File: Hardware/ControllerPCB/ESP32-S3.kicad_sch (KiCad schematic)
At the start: 55 parts, among them J1 UJ20-C-H-G-SMT-1-P16-TR, J4 RJ45, J5 Conn_TagConnect_TC2030-NL_ESP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, J8 Micro_SD_Card, U1 ESP32-S3-WROOM-1, U5 WE-TVS-82400102, U7 AP7333-33SRG-7

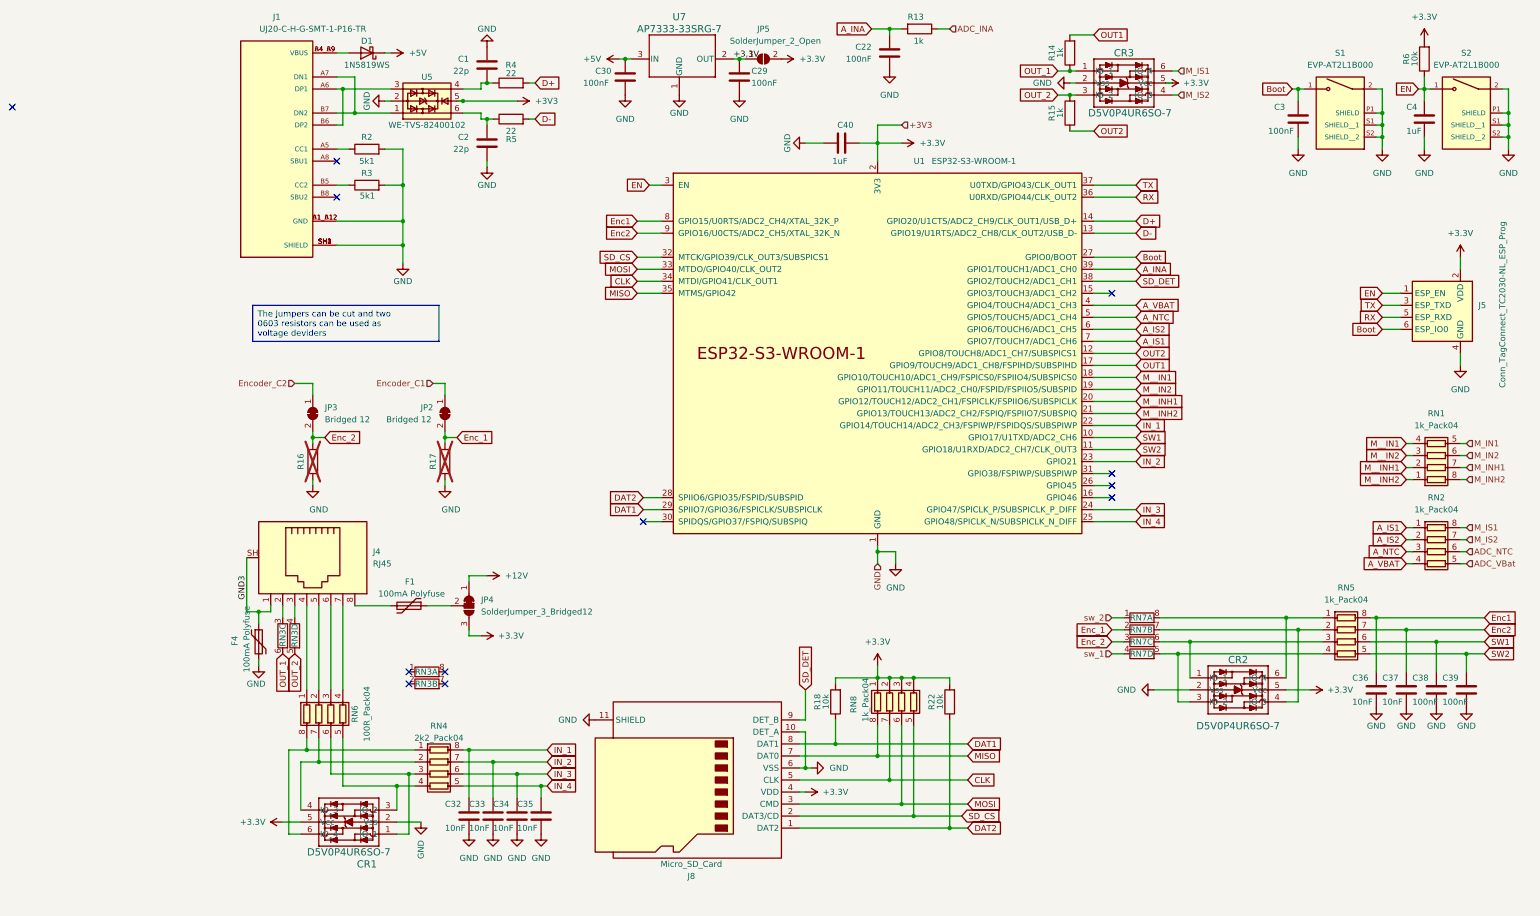
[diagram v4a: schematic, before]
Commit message: update Controller PCB
Add additional capacitor
fix footprint Resistor Array CAT16
fix 3D Model CAT16
change traces from 0.5 to 0.4 mm
fix USB-C Footprint
Export Gerber
update BOM and Values
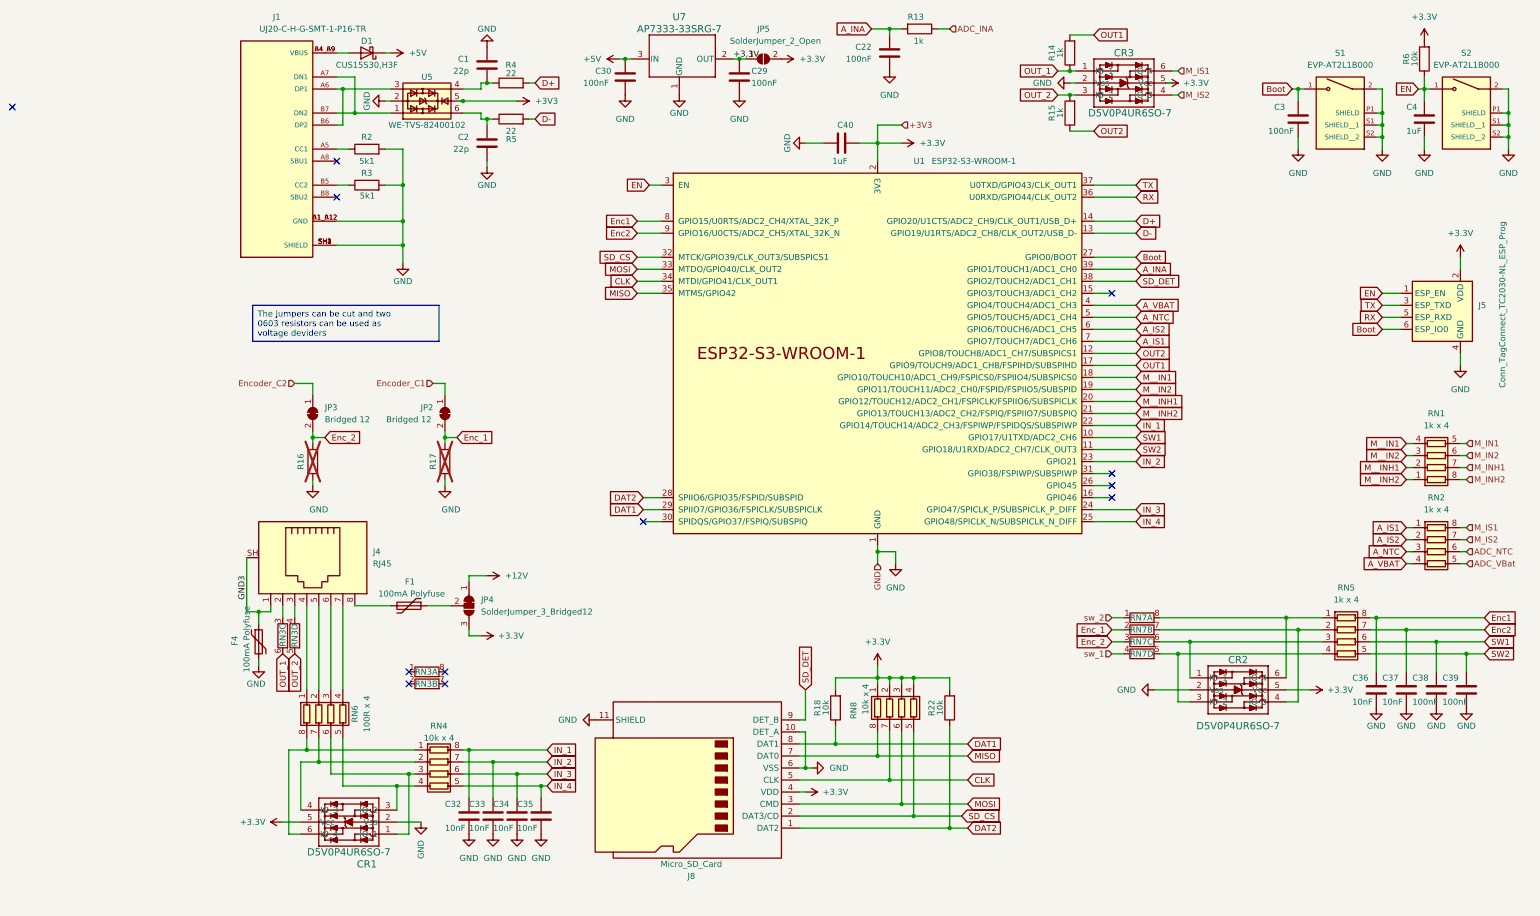
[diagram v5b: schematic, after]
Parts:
- CR1, CR2, CR3: Alternative PN (none) -> D1213A-04SO; Manufacturer_Name (none) -> Diodes Incorporated; Manufacturer_Part_Number (none) -> D5V0P4UR6SO-7; Mouser Part Number (none) -> 621-D5V0P4UR6SO-7; Package (none) -> SOT26; Price (none) -> 0,233
- D1: value 1N5819WS -> CUS15S30,H3F; Manufacturer_Name (none) -> TOSHIBA; Manufacturer_Part_Number (none) -> CUS15S30,H3F; Mouser Part Number (none) -> 757-CUS15S30H3F; Package (none) -> SOD-323-2; Price (none) -> 0,21
- J1: STANDARD Manufacturer Recommendations -> (none); SnapEDA_Link https://www.snapeda.com/parts/UJ20-C-H-G-SMT-1-P16-TR/Same+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 -> (none)
- RN1, RN2, RN5: value 1k_Pack04 -> 1k x 4; footprint BugWiper_lib:BO_CAY16 -> BugWiper_lib:RESCAV80P320X155X60-8N; Manufacturer_Name (none) -> Bourns; Manufacturer_Part_Number (none) -> CAY16-1001F4LF; Mouser Part Number (none) -> 652-CAY16-1001F4LF; Price (none) -> 0,04€
- RN3, RN6, RN7: value 100R_Pack04 -> 100R x 4; footprint BugWiper_lib:BO_CAY16 -> BugWiper_lib:RESCAV80P320X155X60-8N; Manufacturer_Name (none) -> Bourns; Manufacturer_Part_Number (none) -> CAT16A-1000F4LF; Mouser Part Number (none) -> 652-CAT16A-1000F4LF; Price (none) -> 0,10€
- RN4: value 2k2_Pack04 -> 10k x 4; footprint BugWiper_lib:BO_CAY16 -> BugWiper_lib:RESCAV80P320X155X60-8N; Manufacturer_Name (none) -> Bourns; Manufacturer_Part_Number (none) -> CAT16A-1002F4LF; Mouser Part Number (none) -> 652-CAT16A-1002F4LF; Price (none) -> 0,10€
- RN8: value 1k_Pack04 -> 10k x 4; footprint BugWiper_lib:BO_CAY16 -> BugWiper_lib:RESCAV80P320X155X60-8N; Manufacturer_Name (none) -> Bourns; Manufacturer_Part_Number (none) -> CAT16A-1002F4LF; Mouser Part Number (none) -> 652-CAT16A-1002F4LF; Price (none) -> 0,10€
- S1, S2: STANDARD Manufacturer Recommendations -> (none)
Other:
- moved on the sheet: R18, R22, RN8

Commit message: update BOM
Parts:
- removed U5: WE-TVS-82400102, Package_TO_SOT_SMD:SOT-23-6, symbol Power_Protection:WE-TVS-82400102
- added CR4: D5V0P4UR6SO-7, BugWiper_lib:SOT26_DIO, symbol BugWiper_Lib:D5V0P4UR6SO-7
- C1, C2: now not fitted; now left out of the parts list
- C22, C29, C3, C30, C38, C39: value 100nF -> 100nF; Manufacturer_Name (none) -> Samsung; Manufacturer_Part_Number (none) -> CL10B104KB8NNNC; Mouser Part Number (none) -> 187-CL10B104KB8NNNC; Mouser Price/Stock (none) -> 0,01 €
- C32, C33, C34, C35, C36, C37: value 10nF -> 10nF; Manufacturer_Name (none) -> Samsung; Manufacturer_Part_Number (none) -> CL10B103KB8NFNC; Mouser Part Number (none) -> 187-CL10B103KB8NFNC; Mouser Price/Stock (none) -> 0,016 €
- C4: value 1uF -> 100nF; Manufacturer_Name (none) -> Samsung; Manufacturer_Part_Number (none) -> CL10B104KB8NNNC; Mouser Part Number (none) -> 187-CL10B104KB8NNNC; Mouser Price/Stock (none) -> 0,01 €
- C40: value 1uF -> 1uF 50V; footprint Capacitor_SMD:C_0603_1608Metric -> Capacitor_SMD:C_0805_2012Metric
- CR1, CR2, CR3: Mouser Price/Stock (none) -> 0,233€
- D1: Mouser Price/Stock (none) -> 0,209€
- F1, F4: Mouser Part Number (none) -> 504-PTS120630V012; Mouser Price/Stock (none) -> 0,108€
- J1: Mouser Part Number (none) -> 179-UJ20CHGSMT1P16TR; Mouser Price/Stock (none) -> 0,494 €
- J4: Manufacturer_Name (none) -> Amphenol FCI; Manufacturer_Part_Number (none) -> 54602-908LF; Mouser Part Number (none) -> 649-54602-908LF; Mouser Price/Stock (none) -> 0,551 €
- J5: Mouser Price/Stock (none) -> 0€
- J8: Manufacturer_Name (none) -> Molex; Manufacturer_Part_Number (none) -> 104031-0811; Mouser Part Number (none) -> 538-104031-0811; Mouser Price/Stock (none) -> 1,90 €
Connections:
- net +3.3V: now also CR4.5 (Vcc)
- net GND: now also CR4.2 (Vss)
- net at J1.A6 (DP1), J1.B6 (DP2): now also C1.2, R4.1, CR4.3 (IO_2), CR4.4 (IO_3)
- net at J1.A7 (DN1), J1.B7 (DN2): now also C2.1, R5.1, CR4.1 (IO_1), CR4.6 (IO_4)
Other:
- moved on the sheet: R4, R5

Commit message: update
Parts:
- F1, F4: value 100mA Polyfuse -> PTS120630V012
- J1: PARTREV 1.0 -> (none)
- J4: value RJ45 -> 54602-908LF
- J8: value Micro_SD_Card -> 104031-0811
- JP4, JP5: now left out of the parts list
- R13, R14, R15: Manufacturer_Name (none) -> YAGEO; Manufacturer_Part_Number (none) -> RC0603FR-071KL; Mouser Part Number (none) -> 603-RC0603FR-071KL; Mouser Price/Stock (none) -> 0,009 €
- R18, R22, R6: Manufacturer_Name (none) -> YAGEO; Manufacturer_Part_Number (none) -> RC0603FR-1010KL; Mouser Part Number (none) -> 603-RC0603FR-1010KL; Mouser Price/Stock (none) -> 0,008 €
- R2, R3: Manufacturer_Name (none) -> YAGEO; Manufacturer_Part_Number (none) -> RC0603FR-105K1L; Mouser Part Number (none) -> 603-RC0603FR-105K1L; Mouser Price/Stock (none) -> 0,008 €
- R4, R5: Manufacturer_Name (none) -> Bourns; Manufacturer_Part_Number (none) -> CR0603-FX-22R0ELF; Mouser Part Number (none) -> 652-CR0603FX-22R0ELF; Mouser Price/Stock (none) -> 0,009 €
- RN1, RN2, RN5: JLCPCB Part # (none) -> C600863; JLCPCB Price (none) -> 0.0138; Mouser Price/Stock (none) -> 0,034 €
- RN3, RN6, RN7: JLCPCB Part # (none) -> C25506; JLCPCB Price (none) -> 0.0051; Mouser Price/Stock (none) -> 0,098 €
- RN4, RN8: JLCPCB Part # (none) -> C29718; JLCPCB Price (none) -> 0.0053; Mouser Price/Stock (none) -> 0,085 €
- S1, S2: Manufacturer_Part_Number (none) -> EVP-AT2L1B000; Mouser Part Number (none) -> 667-EVP-AT2L1B000; Mouser Price/Stock (none) -> 0,732 €; PARTREV N/A -> (none)
- U1: Manufacturer_Name (none) -> Espressif Systems; Manufacturer_Part_Number (none) -> ESP32-S3-WROOM-1-N16R8; Mouser Part Number (none) -> 356-ESP32S3WRM1N16R8; Mouser Price/Stock (none) -> 3,71 €
- U7: Manufacturer_Name (none) -> Diodes Incorporated; Manufacturer_Part_Number (none) -> AP7333-33SRG-7; Mouser Part Number (none) -> 621-AP7333-33SRG-7; Mouser Price/Stock (none) -> 0,314 €

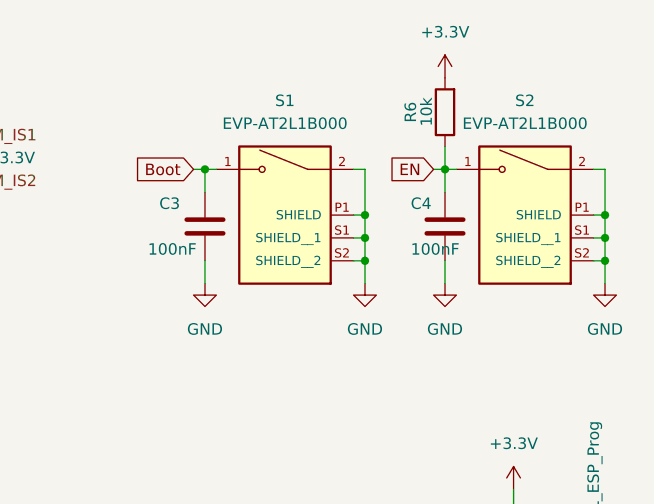
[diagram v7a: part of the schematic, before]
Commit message: update PCB and Gerber
change Switches to cheaper ones
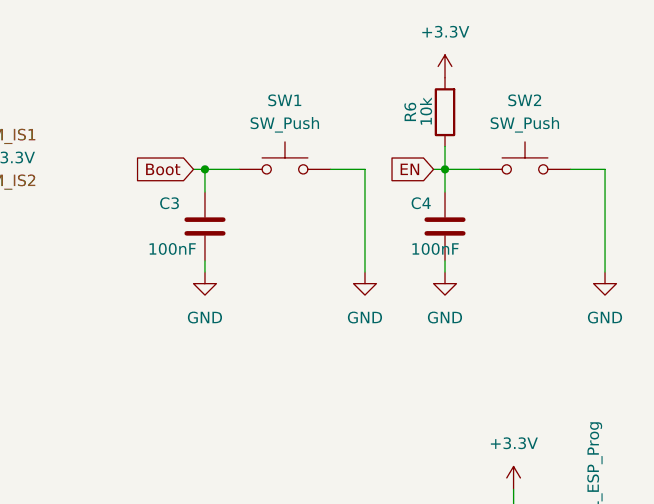
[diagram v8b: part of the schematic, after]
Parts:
- removed S1, S2: EVP-AT2L1B000, BugWiper_lib:SW_EVP-AT2L1B000, symbol BugWiper_Lib:EVP-AT2L1B000
- added SW1, SW2: SW_Push, BugWiper_lib:EVQ9P701P, symbol Switch:SW_Push
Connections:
- net Boot: now also SW1.1
- net EN: now also SW2.1
- net GND: now also SW1.2, SW2.2
